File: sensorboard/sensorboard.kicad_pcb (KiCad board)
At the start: 2 copper layers, 100 x 50 mm, 231 parts, among them J1 Conn_01x03, J10 Conn_01x02_Male, J11 Conn_01x05_Male, J12 Conn_01x03, J13 Conn_01x03, J14 USB_C_Receptacle_USB2.0, J2 Conn_01x03, J3 Conn_01x03, J4 Conn_01x03, J5 Conn_01x03, J6 Conn_01x03, J7 Conn_01x03, J8 Conn_01x03, J9 Conn_01x02_Male, Q1 MMDT2222A, U1 ESP32-PICO-D4, U10 MAX31856, U11 MAX31856, U12 RT9025-25GSP, U13 ADS1219, U14 ADS1219, U15 ADS1219, U16 MAX31856, U17 MAX31856, U18 MAX31856, U19 LTC4411, U2 LTC4411, U20 SN65HVD230, U3 TPS61092RSAR, U4 MAX31856, U5 MAX31856, U6 MAX31856, U7 MAX31856, U8 CP2102-GMR-QFN28, U9 MAX31856

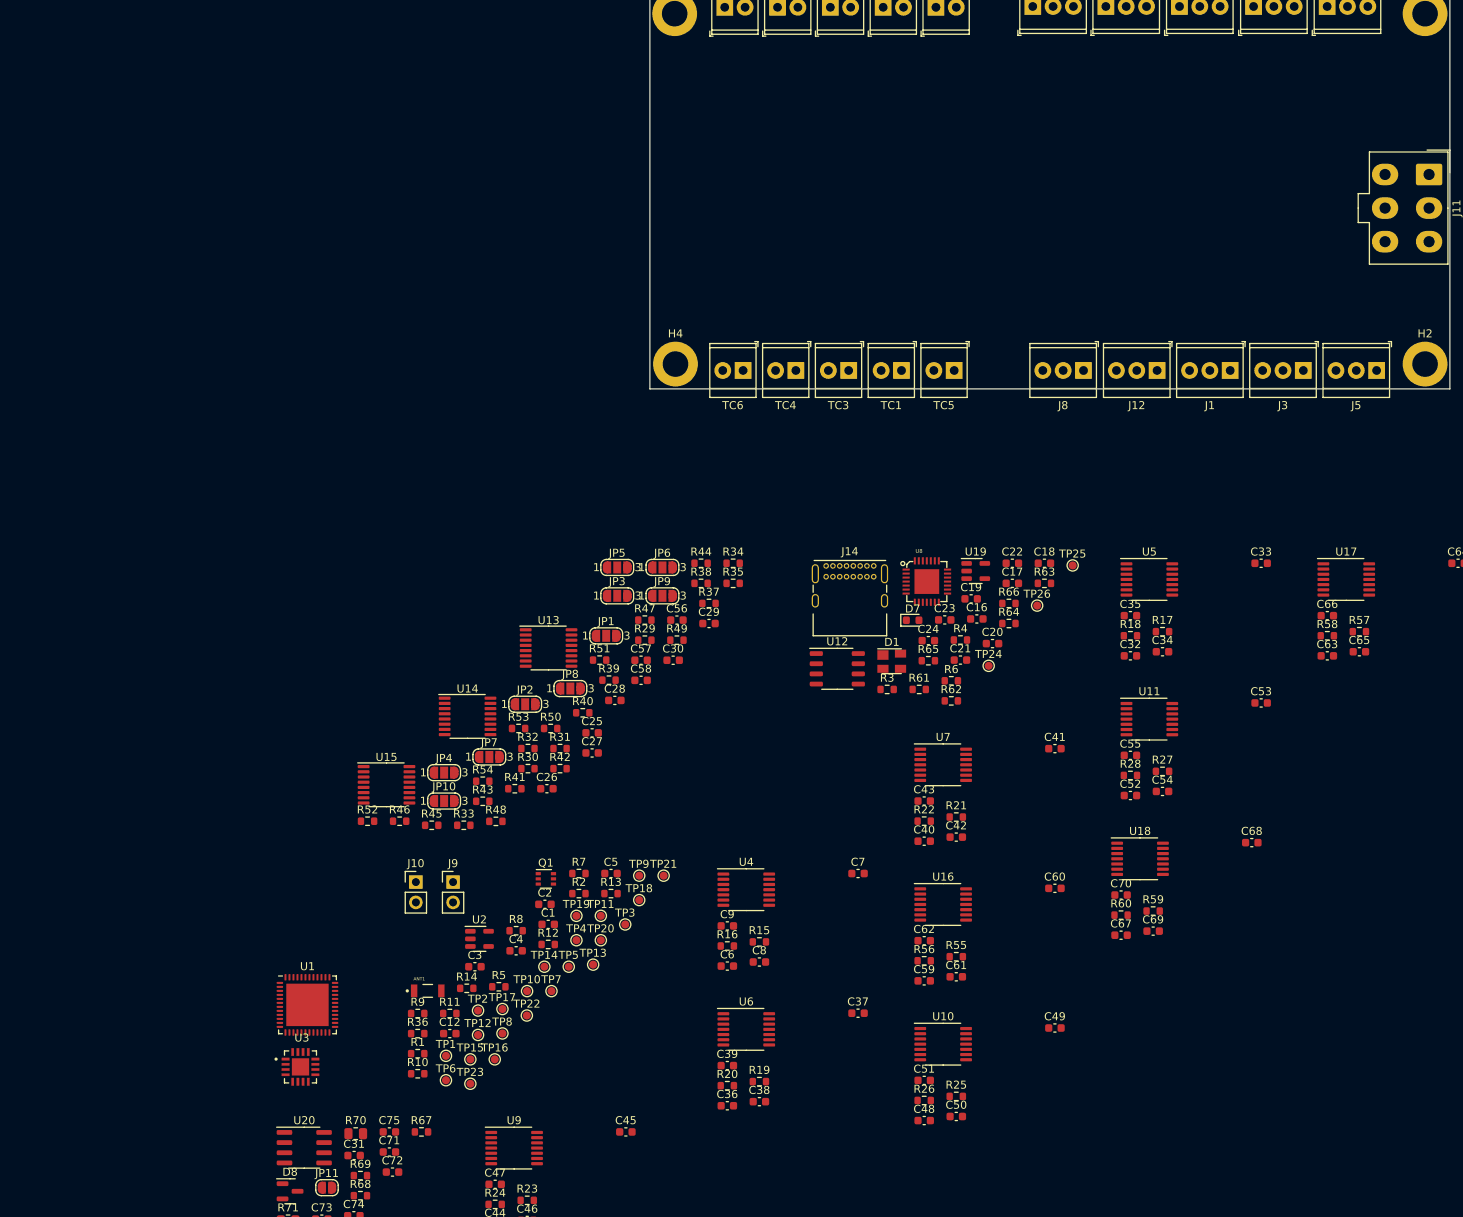
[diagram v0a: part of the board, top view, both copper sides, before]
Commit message: Stackup + capacitor fps
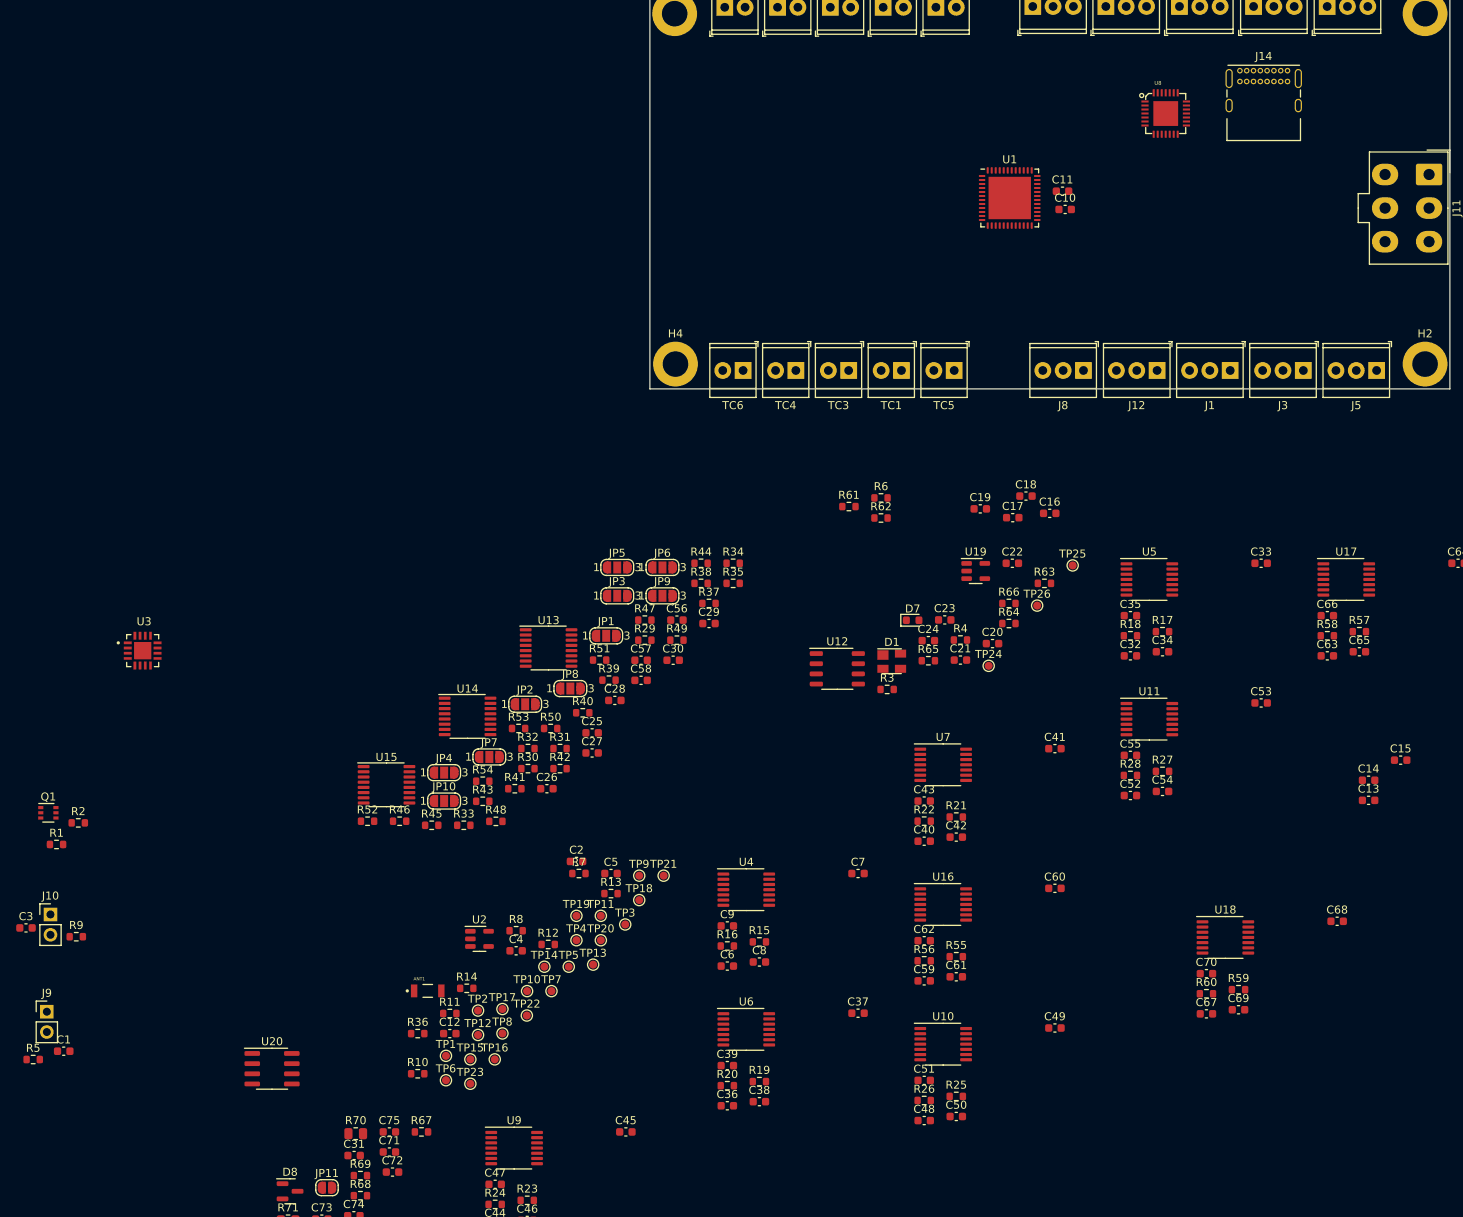
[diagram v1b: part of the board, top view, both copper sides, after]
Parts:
- added C10: 10uF, Capacitor_SMD:C_0603_1608Metric, F.Cu at (151.9, 57.6)
- added C11: 100nF, Capacitor_SMD:C_0603_1608Metric, F.Cu at (151.6, 55.3)
- added C13: 10uF, Capacitor_SMD:C_0603_1608Metric, F.Cu at (189.8, 131.4)
- added C14: 2.2uF, Capacitor_SMD:C_0603_1608Metric, F.Cu at (189.8, 128.9)
- added C15: 100uF, Capacitor_SMD:C_0603_1608Metric, F.Cu at (193.8, 126.4)
- moved U1 133.7 mm to (145.0, 56.1)
- moved J14 80.7 mm to (173.8, 40.2)
- moved U8 65.7 mm to (164.5, 45.6)
- moved R2 63.2 mm to (28.6, 134.2)
- moved Q1 62.7 mm to (24.8, 133.0)
- moved C1 62.6 mm to (26.7, 162.8)
- moved R5 58.9 mm to (22.9, 163.8)
- moved C3 56.3 mm to (22.0, 147.4)
- moved U3 55.6 mm to (36.6, 112.7)
- moved J9 53.3 mm to (24.6, 157.9)
- moved R1 52.2 mm to (25.8, 136.9)
- moved J10 45.9 mm to (25.1, 145.7)
- moved R9 43.7 mm to (28.3, 148.5)
- moved R6 24.5 mm to (128.9, 93.6)
- moved R62 24.5 mm to (128.9, 96.1)
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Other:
- copper layers 2 -> 4

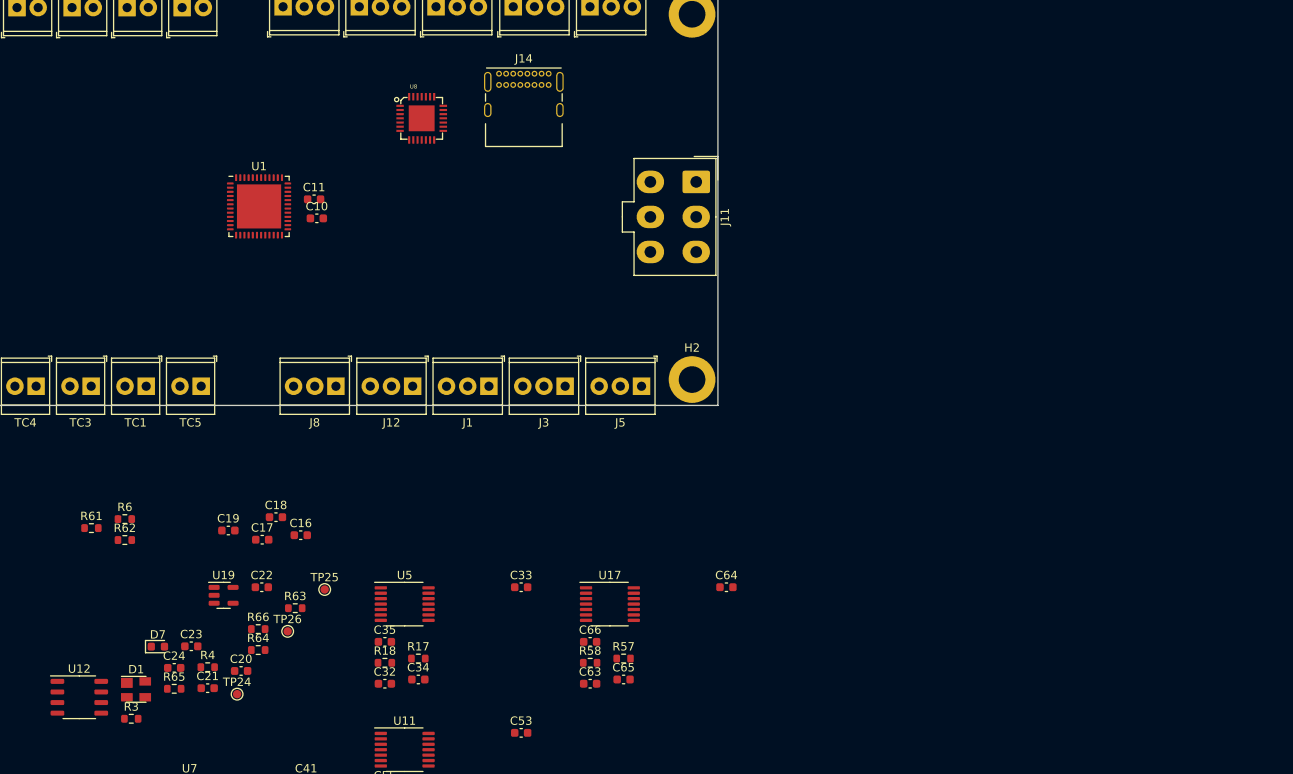
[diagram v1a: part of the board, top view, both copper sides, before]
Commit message: usb-uart structure done
Original FPs were used, copies from usb were deleted, however the structure was kept the same
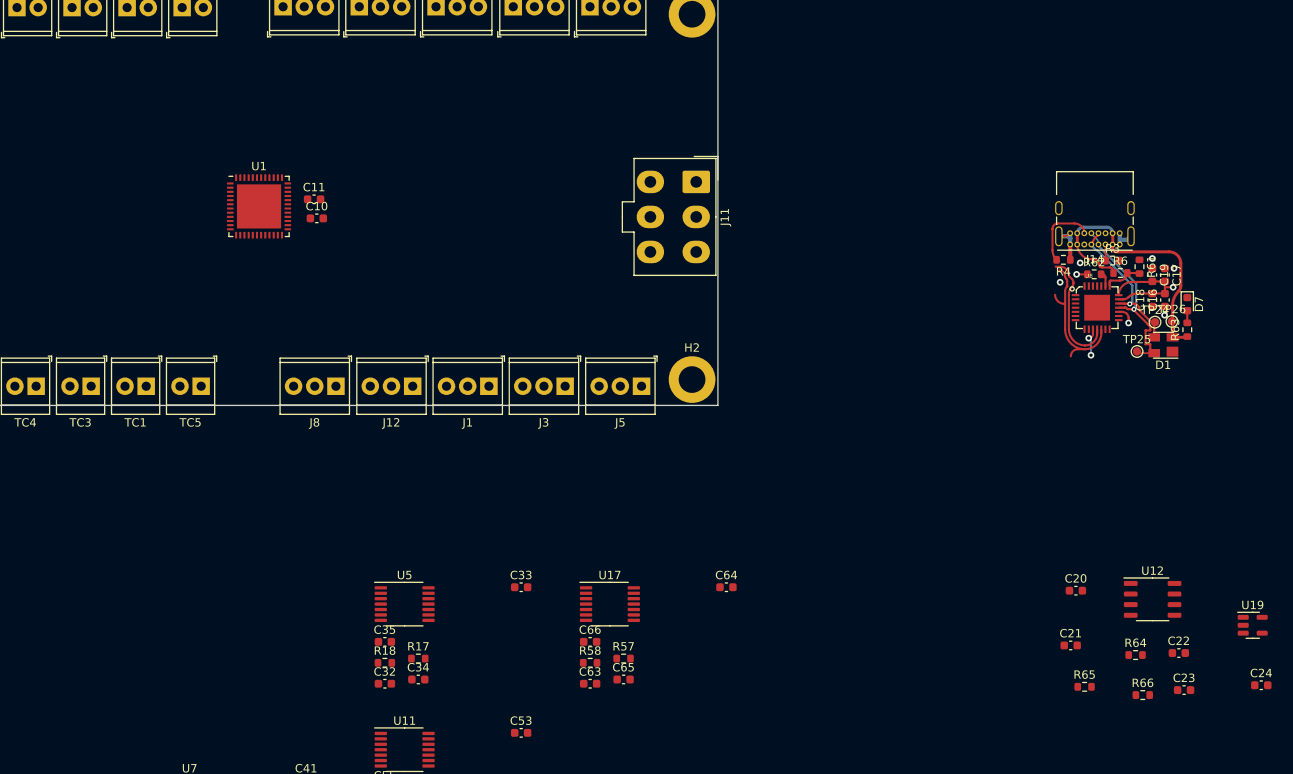
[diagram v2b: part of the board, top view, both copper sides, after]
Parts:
- moved C24 130.4 mm to (265.1, 113.5)
- moved D7 130.1 mm to (256.3, 67.9), turned to -90 degrees
- moved D1 129.9 mm to (253.4, 72.8), turned to 180 degrees
- moved R3 129.8 mm to (247.3, 62.6)
- moved R61 129.5 mm to (250.5, 63.4), turned to -90 degrees
- moved U12 129.2 mm to (252.1, 103.2)
- moved U19 123.4 mm to (264.1, 106.4)
- moved R6 123.0 mm to (248.3, 64.1)
- moved R62 120.5 mm to (245.1, 64.3)
- moved C23 119.2 mm to (255.9, 114.1)
- moved TP24 118.8 mm to (252.4, 70.0)
- moved C19 114.9 mm to (252.1, 64.4), turned to -90 degrees
- moved R4 113.6 mm to (241.4, 62.5), turned to 180 degrees
- moved C17 112.8 mm to (253.6, 64.4), turned to -90 degrees
- moved TP26 112.4 mm to (254.4, 69.9)
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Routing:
- net VBUS: track 0.00 -> 34.2 mm
- net /usb/Data+: track 0.00 -> 22.3 mm
- net /usb/Data-: track 0.00 -> 19.8 mm
- net unconnected-(U8-Pad12): track 0.00 -> 18.4 mm
- net +3V3: track 0.00 -> 15.4 mm, vias 0 -> 2
- net unconnected-(U8-Pad11): track 0.00 -> 14.6 mm
- net GND: track 0.00 -> 8.97 mm, vias 0 -> 6
- net Net-(J14-PadB5): track 0.00 -> 8.62 mm
- net unconnected-(U8-Pad22): track 0.00 -> 4.60 mm
- net unconnected-(U8-Pad10): track 0.00 -> 3.52 mm
- net unconnected-(U8-Pad17): track 0.00 -> 2.18 mm
- net Net-(J14-PadA5): track 0.00 -> 1.93 mm
- net Net-(R17-Pad2): track 0.00 -> 1.78 mm
- net Net-(D7-Pad2): track 0.00 -> 1.45 mm
- net /RTS: vias 0 -> 2
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
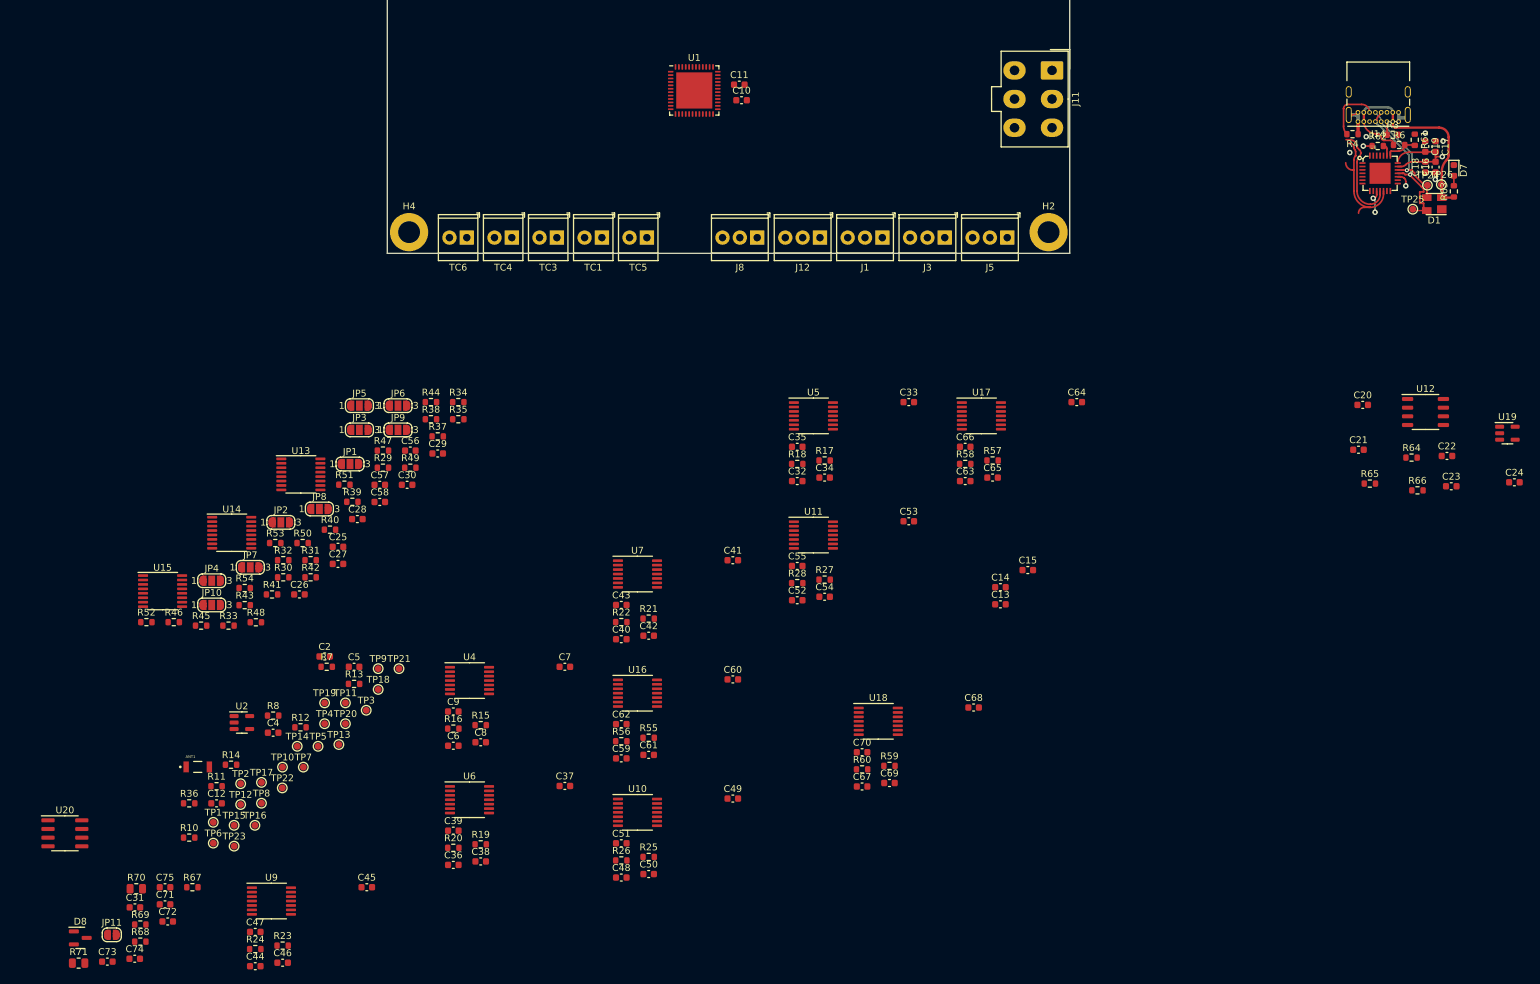
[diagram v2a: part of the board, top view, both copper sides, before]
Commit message: CAN structure done
Main structure copied across from actuator board, fps from sensor board used
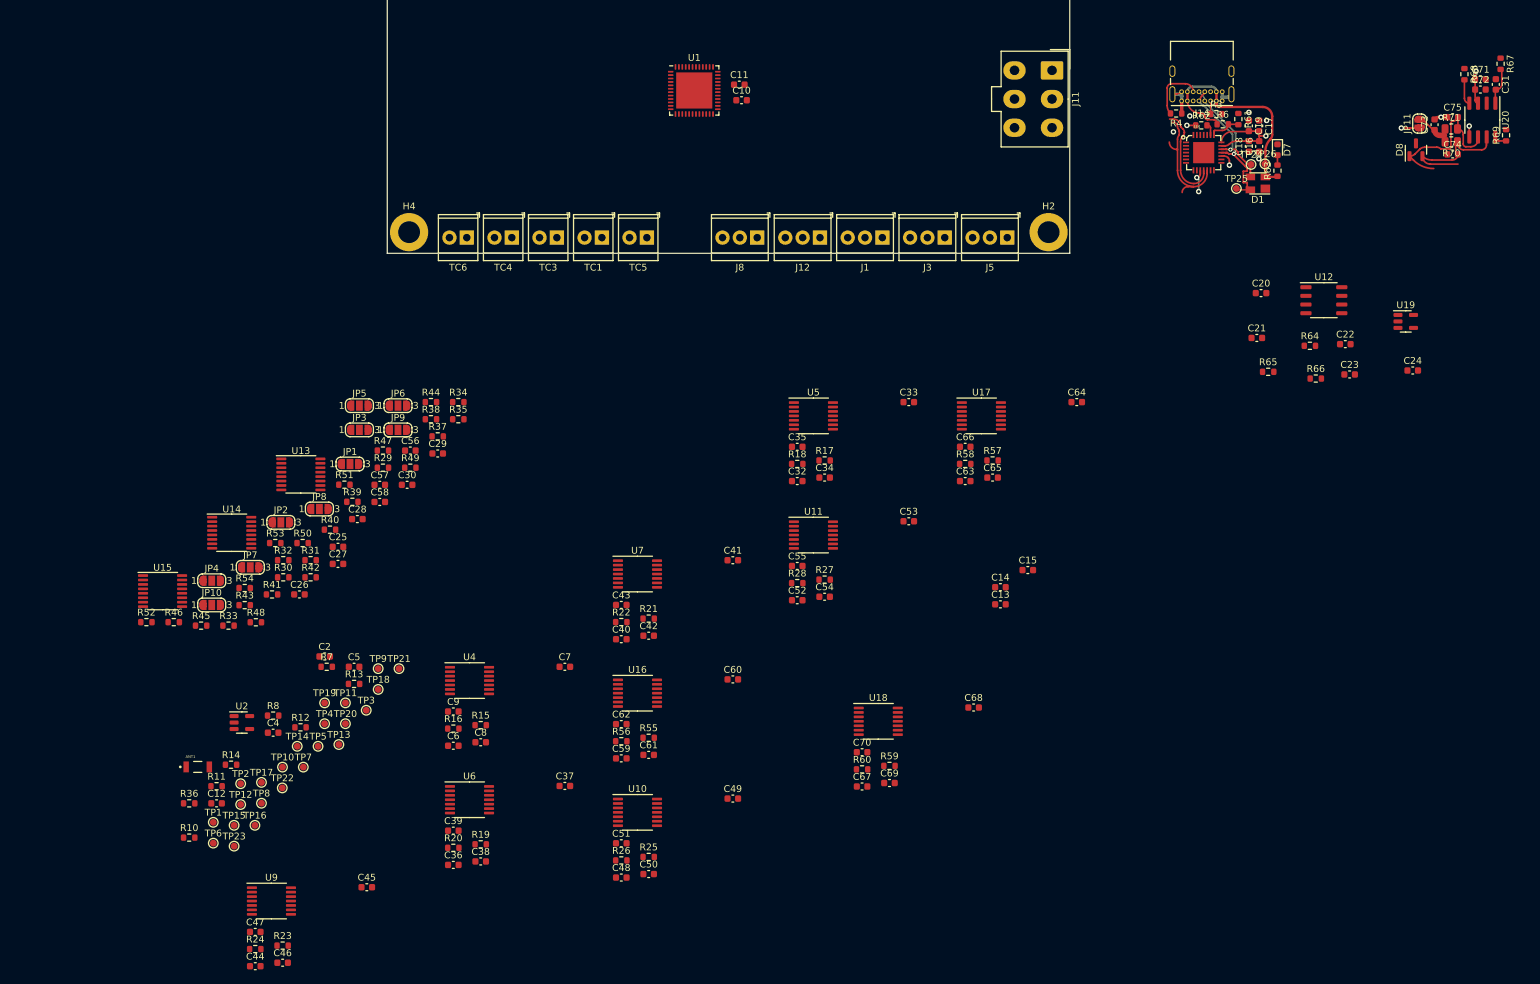
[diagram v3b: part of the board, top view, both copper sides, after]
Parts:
- moved R71 235.3 mm to (255.9, 61.8)
- moved C31 233.0 mm to (262.4, 55.3), turned to -90 degrees
- moved U20 232.5 mm to (260.4, 60.5), turned to -90 degrees
- moved R68 231.9 mm to (257.8, 53.8), turned to -90 degrees
- moved R69 231.1 mm to (263.9, 62.7), turned to 90 degrees
- moved C73 229.9 mm to (253.4, 61.2), turned to 90 degrees
- moved C72 227.7 mm to (260.2, 56.0)
- moved C71 227.5 mm to (260.2, 54.5)
- moved D8 227.2 mm to (250.7, 64.8), turned to 90 degrees
- moved R67 226.5 mm to (263.1, 52.2), turned to -90 degrees
- moved C74 226.2 mm to (256.1, 65.5)
- moved JP11 225.5 mm to (251.2, 61.0), turned to 90 degrees
- moved R70 221.6 mm to (255.9, 63.7), turned to 180 degrees
- moved C75 219.8 mm to (256.1, 60.1)
- moved C17 26.0 mm to (227.8, 61.3)
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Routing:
- net /CAN_LOW: track 0.00 -> 23.0 mm
- net /CAN_HIGH: track 0.00 -> 18.9 mm
- net Net-(C31-Pad2): track 0.00 -> 5.16 mm
- net Net-(C73-Pad1): track 0.00 -> 4.71 mm
- net +3V3: track 15.4 -> 20.0 mm, vias 2 -> 3
- net /CAN/Vref: track 0.00 -> 4.25 mm, vias 0 -> 2
- net Net-(R68-Pad2): track 0.00 -> 3.81 mm
- net Net-(R69-Pad1): track 0.00 -> 1.88 mm
- net GND: track 8.97 -> 10.8 mm, vias 6 -> 7
